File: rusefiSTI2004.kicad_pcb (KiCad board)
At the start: 4 copper layers, 138.6 x 113.6 mm, 128 parts, among them J1 TE_1-1376430-0, J2 USB C 2.0 16P, J3 Molex_39281143, M1 Module-mega-mcu144-0.7, M10 Module-lin-0.1, M11 Module-dinput4-0.1, M12 Module-dinput4-0.1, M13 Module-knock-0.2, M14 Module-power_12and5V-0.3, M2 Module-motor-driver-0.1, M3 Module-wbo-0.5, M5 Module-vr-discrete-0.5, M8 Module-power_12and5V-0.3, M9 Module-motor-driver-0.1, P1 WBO_UN, P10 OUT_SPARE_LS2, P11 CHARGE_A22, P12 FP_STATUS, P13 DLC6_D29, P14 SPARE_IGN6, P15 SPARE_IGN7, P16 SPARE_IGN8, P17 I2C_1_SCL, P18 I2C_1_SDA, P19 +5VA, P2 WBO_VM, P20 +3.3V, P21 +12V_RAW, P22 GND, P23 BOOT0, P24 SWDIO, P25 SWCLK, P26 NRST, P27 SPARE_PWM3, P28 SPARE_RES2, P29 AUX_IN1, P3 WBO_IP, P30 AUX_IN2, P31 AUX_IN3, P32 PG_5VP_APS, P4 WBO_RTRIM, P5 WBO_HEATER, P6 CAN_H, P7 CAN_L, P8 K_LINE, P9 OUT_SPARE_LS1, Q16 NCV8401BDTRKG, U1 USBLC6-2SC6, U10 VNLD5160TR-E, U11 VNLD5160TR-E, U12 VNLD5160TR-E, U13 VNLD5160TR-E, U14 VNLD5160TR-E, U15 VNLD5160TR-E, U16 VNLD5160TR-E, U17 VNLD5160TR-E, U18 VNLD5160TR-E, U19 VNLD5160TR-E

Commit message: Stage 2 routing: ETB, TGV, WBO and rear O2 heater paths (kicad-autoroute)
DRC 0 errors, bends under 135 deg 0, unconnected 326 -> 320, parity 0.
Rules: SMD pads need one thermal spoke; track_angle is a warning because
T-junctions always trip it (bends are enforced by kicad-autoroute).

Co-Authored-By: Claude Opus 5.5 <noreply@anthropic.com>
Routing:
- net OUT_ETB-: track 0.00 -> 111.8 mm, vias 0 -> 1
- net +12V_ETB: track 0.00 -> 111.5 mm
- net WBO_HEATER: track 0.00 -> 87.3 mm
- net OUT_TGV_CLOSE: track 0.00 -> 80.0 mm, vias 0 -> 1
- net OUT_O2_HEATER_REAR: track 0.00 -> 69.4 mm
- net OUT_TGV_OPEN: track 0.00 -> 4.61 mm
- net GND: vias 74 -> 0

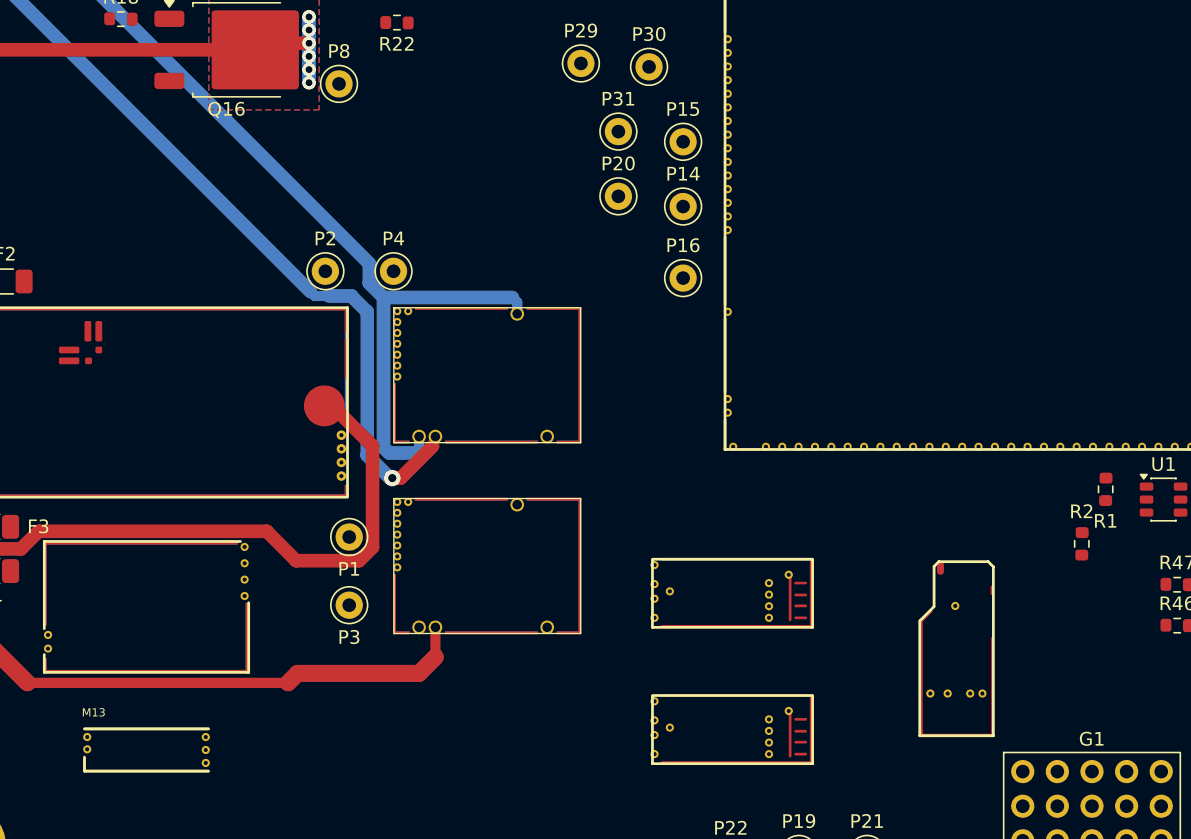
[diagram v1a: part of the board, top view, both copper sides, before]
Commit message: On-board MAP sensor (AlphaX style): U20 MPXHZ6400AC6T1 + C1 100n on +5VA -> M1 IN_MAP3 (S19)
TGV position RH moves from IN_MAP3 to IN_RES2 (S14). J3 pin 8 (was AUX_AN1 on
IN_RES2) is now not connected; P28 is the MAP test pad. External MAP stays on
IN_MAP1. PCB: U20/C1 placed left of M1, DRC 0 errors, unconnected 322.

Co-Authored-By: Claude Opus 5.5 <noreply@anthropic.com>
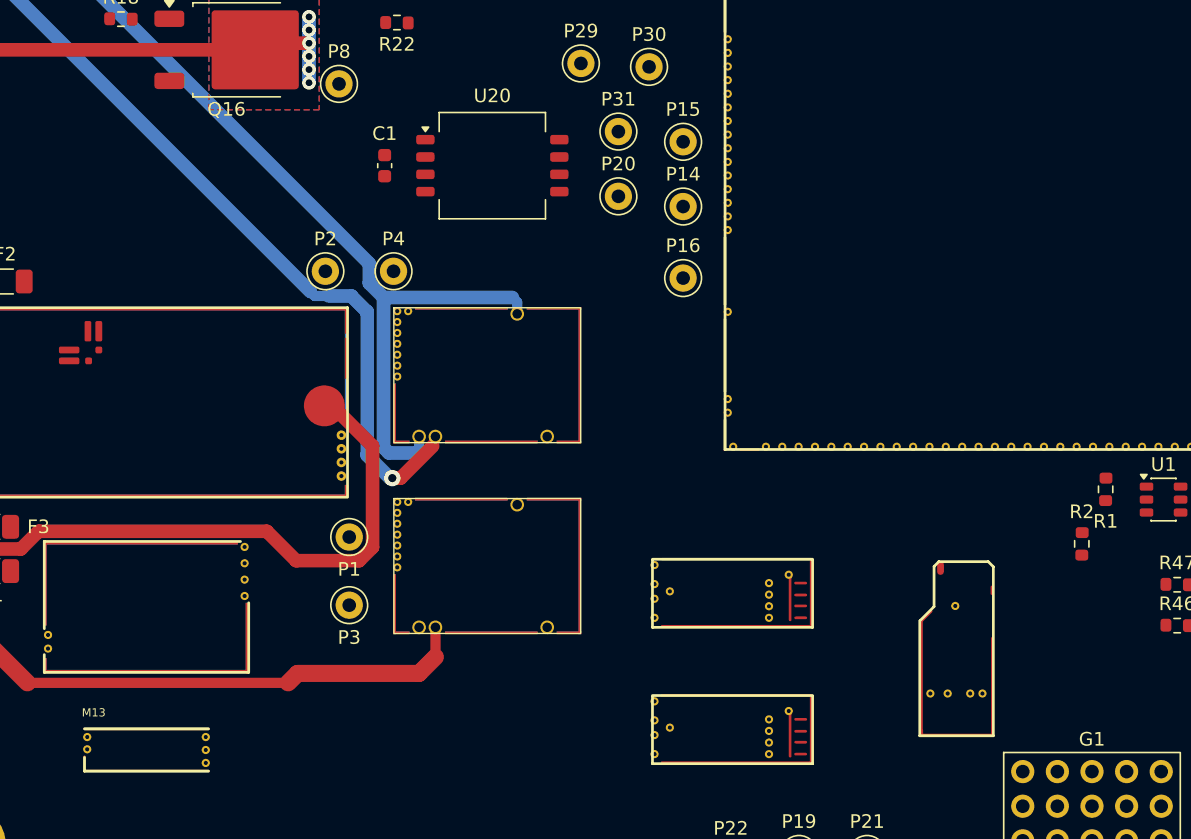
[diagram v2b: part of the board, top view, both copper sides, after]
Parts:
- added C1: 100n_50V_X7R, EmbeddedEra_Library:C_0603_1608Metric, F.Cu at (154.6, 95.5)
- added U20: MPXH6400A, EmbeddedEra_Library:PRESSURE_8-SSOP, F.Cu at (162.5, 95.5)
- P28: value SPARE_RES2 -> MAP_ONBOARD
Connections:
- J3 pad 8: SPARE_RES2 -> unconnected-(J3-Pin_8-Pad8)
- M1 pad S14: SPARE_RES2 -> IN_TUMBLE_SENSOR_RH
- M1 pad S19: IN_TUMBLE_SENSOR_RH -> IN_MAP_ONBOARD
- P28 pad 1: SPARE_RES2 -> IN_MAP_ONBOARD

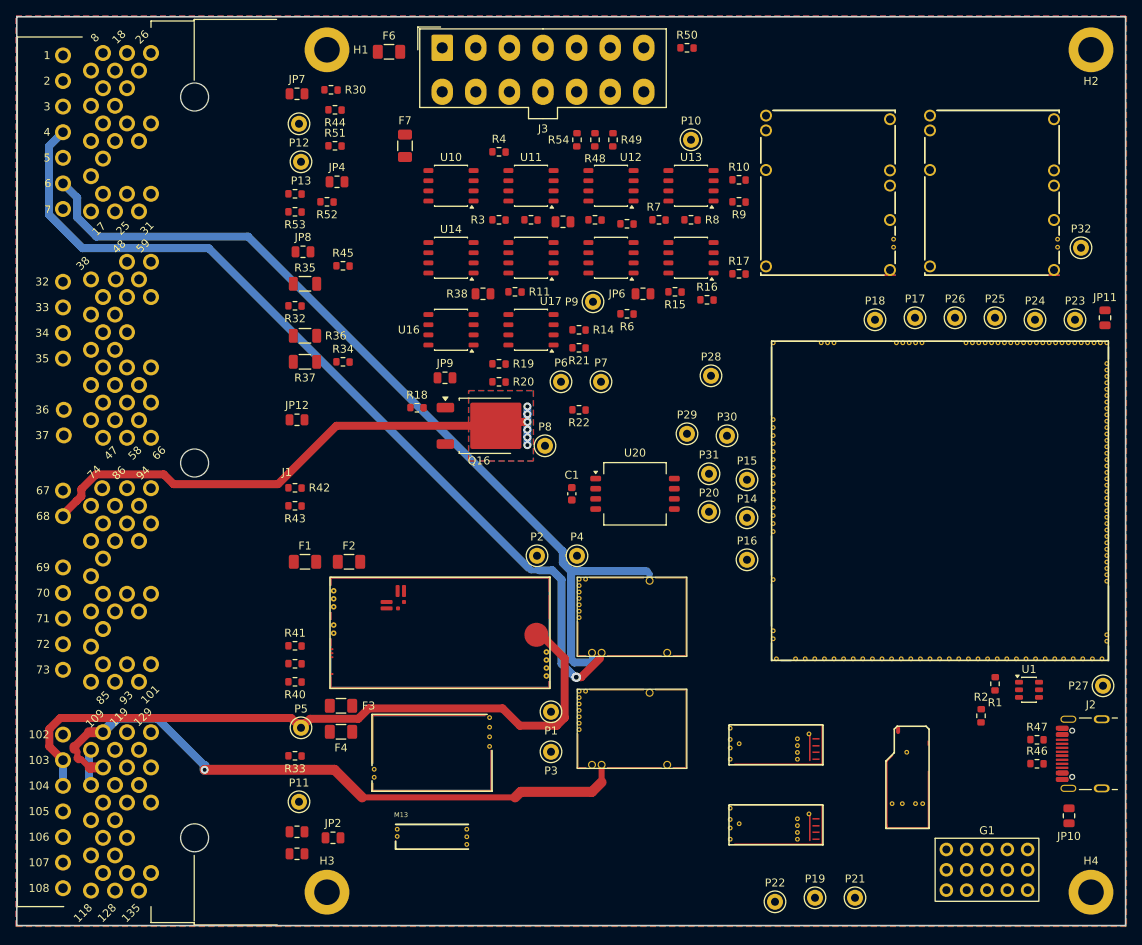
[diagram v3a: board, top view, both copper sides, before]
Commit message: Stage 2 rerouted: all 7 high-current nets routed, wider tracks; U20 out of the ETB corridor
The 2026-10-13 pass had left OUT_ETB+ and OUT_TGV_OPEN unrouted. Routed at
0.8 mm (fits between J1 pins), widened with local necking, small parts nudged
off the wide tracks (F3 F4 P2 P4 R33 R34 R36 R37). U20 moves to the gap east of
M2, C1 under its supply pins. DRC 0 errors, bends 0, unconnected 324.

Co-Authored-By: Claude Opus 5.5 <noreply@anthropic.com>
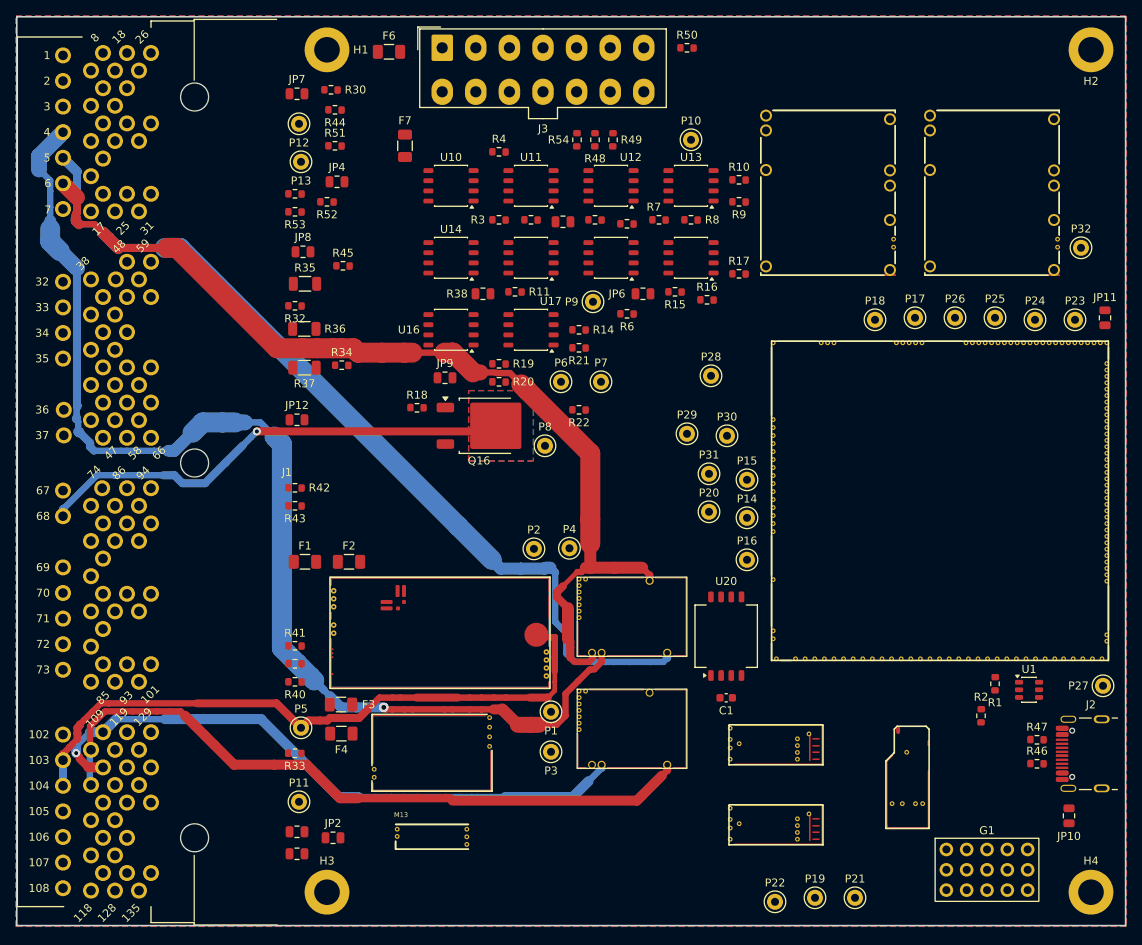
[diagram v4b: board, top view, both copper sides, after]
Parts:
- moved C1 32.0 mm to (173.9, 121.0), turned to 0 degrees
- moved U20 21.1 mm to (173.9, 113.3), turned to 90 degrees
- moved P4 1.33 mm to (154.3, 102.3)
- moved P2 0.95 mm to (149.9, 102.4)
- moved R36 0.87 mm to (121.2, 74.9)
- moved R37 0.73 mm to (121.2, 79.7)
- moved R34 0.45 mm to (125.8, 79.4)
- moved R33 0.32 mm to (120.0, 127.9)
- moved F4 0.23 mm to (125.8, 125.5)
- moved F3 0.16 mm to (125.7, 121.8)
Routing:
- net OUT_ETB+: track 0.00 -> 111.5 mm
- net OUT_TGV_OPEN: track 4.61 -> 87.3 mm
- net OUT_ETB-: track 111.8 -> 145.6 mm
- net +12V_ETB: track 111.5 -> 123.1 mm
- net OUT_O2_HEATER_REAR: track 69.4 -> 60.1 mm, vias 6 -> 1
- net WBO_HEATER: track 87.3 -> 80.9 mm
- net OUT_TGV_CLOSE: track 80.0 -> 78.1 mm
